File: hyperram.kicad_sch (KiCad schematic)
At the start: 7 parts

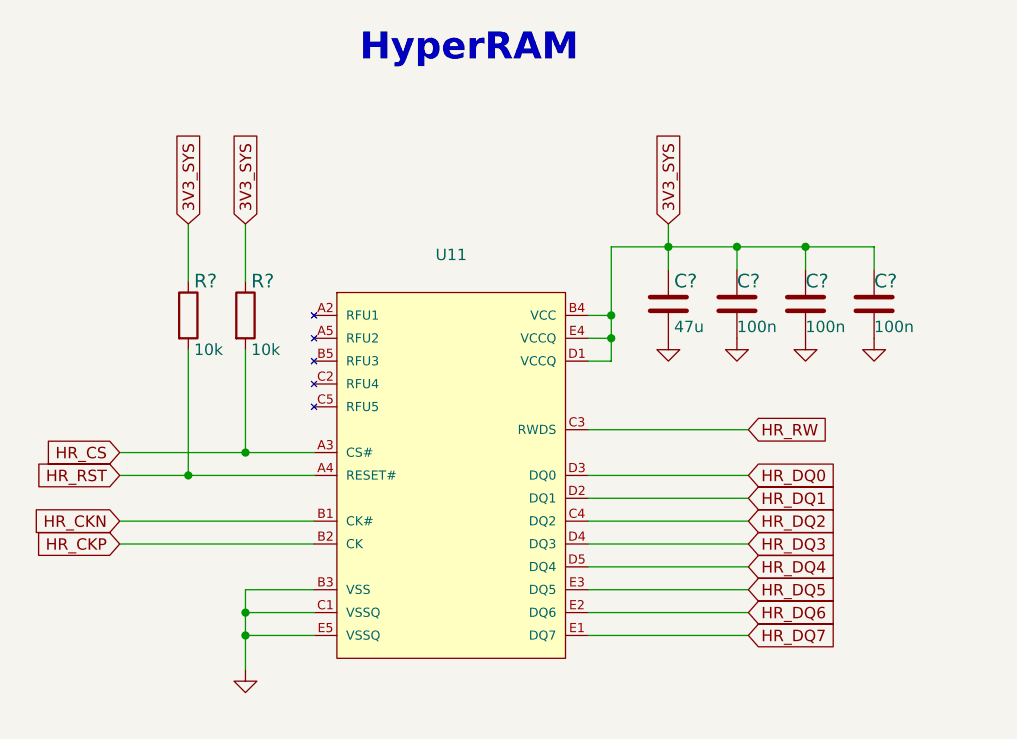
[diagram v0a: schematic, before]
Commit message: Added EN pullup for TPS54561 to avoid disabling by touch
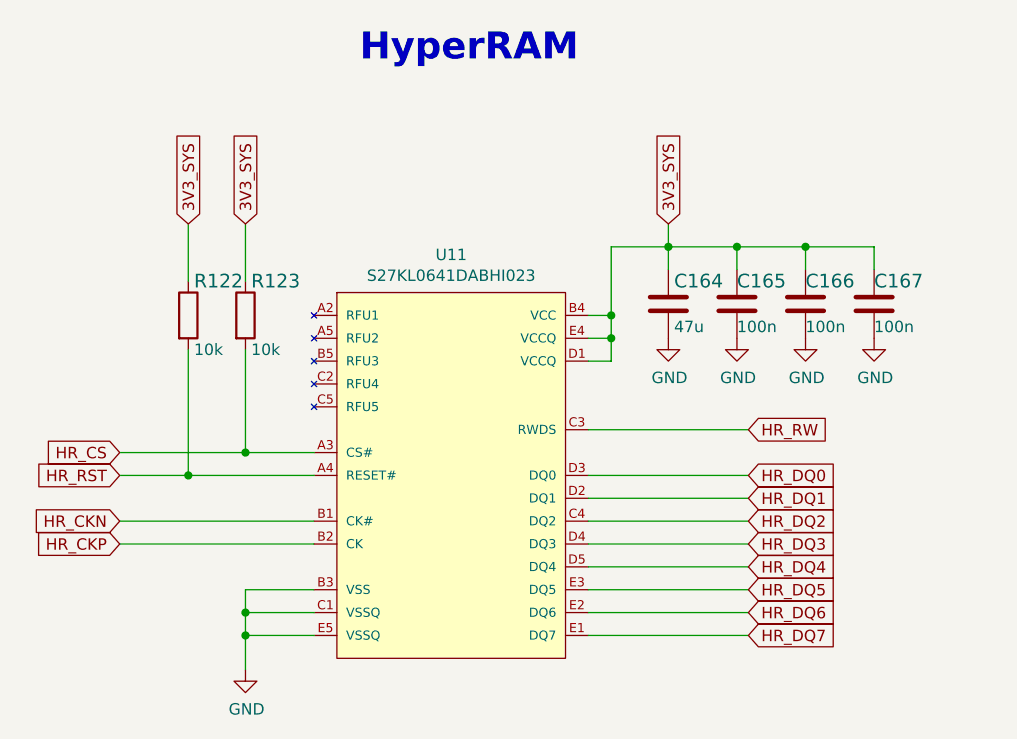
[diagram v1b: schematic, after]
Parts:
- C164: renamed from C?; value (none) -> C_47u_0603; footprint (none) -> ddr5-testboard-footprints:0603-cap
- C165, C166, C167: renamed from C?; value (none) -> C_100n_0402_6V3; footprint (none) -> ddr5-testboard-footprints:0402-cap
- R122, R123: renamed from R?; value (none) -> R_10k_0402; footprint (none) -> ddr5-testboard-footprints:0402-res
- U11: value (none) -> S27KL0641DABHI023; footprint (none) -> ddr5-testboard-footprints:FBGA-24
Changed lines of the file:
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@@
     (in_bom yes) (on_board yes)
     (property "Reference" "U11" (id 0) (at 196.215 125.984 0))
-    (property "Value" "" (id 1) (at 196.215 128.2954 0))
-    (property "Footprint" "" (id 2) (at 184.785 178.435 0)
+    (property "Value" "S27KL0641DABHI023" (id 1) (at 196.215 128.2954 0))
+    (property "Footprint" "ddr5-testboard-footprints:FBGA-24" (id 2) (at 184.785 178.435 0)
       (effects (font (size 1.27 1.27)) (justify left bottom) hide)
     )
@@
   (symbol (lib_id "ddr5-testboard:C_47u_0603") (at 220.345 131.445 0) (unit 1)
     (in_bom yes) (on_board yes)
-    (property "Reference" "C?" (id 0) (at 220.98 128.905 0)
-      (effects (font (size 1.524 1.524)) (justify left))
-    )
-    (property "Value" "" (id 1) (at 220.345 135.255 0)
-      (effects (font (size 1.524 1.524)) hide)
-    )
-    (property "Footprint" "" (id 2) (at 225.425 126.365 0)
+    (property "Reference" "C164" (id 0) (at 220.98 128.905 0)
+      (effects (font (size 1.524 1.524)) (justify left))
+    )
+    (property "Value" "C_47u_0603" (id 1) (at 220.345 135.255 0)
+      (effects (font (size 1.524 1.524)) hide)
+    )
+    (property "Footprint" "ddr5-testboard-footprints:0603-cap" (id 2) (at 225.425 126.365 0)
       (effects (font (size 1.524 1.524)) (justify left) hide)
     )
@@
   (symbol (lib_id "ddr5-testboard:C_100n_0402_6V3") (at 235.585 131.445 0) (unit 1)
     (in_bom yes) (on_board yes)
-    (property "Reference" "C?" (id 0) (at 235.585 128.905 0)
-      (effects (font (size 1.524 1.524)) (justify left))
-    )
-    (property "Value" "" (id 1) (at 235.585 135.255 0)
-      (effects (font (size 1.524 1.524)) hide)
-    )
-    (property "Footprint" "" (id 2) (at 240.665 126.365 0)
+    (property "Reference" "C166" (id 0) (at 235.585 128.905 0)
+      (effects (font (size 1.524 1.524)) (justify left))
+    )
+    (property "Value" "C_100n_0402_6V3" (id 1) (at 235.585 135.255 0)
+      (effects (font (size 1.524 1.524)) hide)
+    )
+    (property "Footprint" "ddr5-testboard-footprints:0402-cap" (id 2) (at 240.665 126.365 0)
       (effects (font (size 1.524 1.524)) (justify left) hide)
     )
@@
   (symbol (lib_id "ddr5-testboard:GND") (at 220.345 135.255 0) (unit 1)
     (in_bom yes) (on_board yes)
-    (property "Reference" "#PWR?" (id 0) (at 220.345 141.605 0)
-      (effects (font (size 1.27 1.27)) hide)
-    )
-    (property "Value" "" (id 1) (at 220.472 139.6492 0))
+    (property "Reference" "#PWR0189" (id 0) (at 220.345 141.605 0)
+      (effects (font (size 1.27 1.27)) hide)
+    )
+    (property "Value" "GND" (id 1) (at 220.472 139.6492 0))
     (property "Footprint" "" (id 2) (at 220.345 135.255 0)
       (effects (font (size 1.27 1.27)) hide)
@@
   (symbol (lib_id "ddr5-testboard:R_10k_0402") (at 167.005 132.715 270) (unit 1)
     (in_bom yes) (on_board yes)
-    (property "Reference" "R?" (id 0) (at 167.64 128.905 90)
-      (effects (font (size 1.524 1.524)) (justify left))
-    )
-    (property "Value" "" (id 1) (at 163.195 132.715 0)
-      (effects (font (size 1.524 1.524)) hide)
-    )
-    (property "Footprint" "" (id 2) (at 172.085 137.795 0)
+    (property "Reference" "R122" (id 0) (at 167.64 128.905 90)
+      (effects (font (size 1.524 1.524)) (justify left))
+    )
+    (property "Value" "R_10k_0402" (id 1) (at 163.195 132.715 0)
+      (effects (font (size 1.524 1.524)) hide)
+    )
+    (property "Footprint" "ddr5-testboard-footprints:0402-res" (id 2) (at 172.085 137.795 0)
       (effects (font (size 1.524 1.524)) (justify left) hide)
     )
@@
   (symbol (lib_id "ddr5-testboard:GND") (at 227.965 135.255 0) (unit 1)
     (in_bom yes) (on_board yes)
-    (property "Reference" "#PWR?" (id 0) (at 227.965 141.605 0)
-      (effects (font (size 1.27 1.27)) hide)
-    )
-    (property "Value" "" (id 1) (at 228.092 139.6492 0))
+    (property "Reference" "#PWR0190" (id 0) (at 227.965 141.605 0)
+      (effects (font (size 1.27 1.27)) hide)
+    )
+    (property "Value" "GND" (id 1) (at 228.092 139.6492 0))
     (property "Footprint" "" (id 2) (at 227.965 135.255 0)
       (effects (font (size 1.27 1.27)) hide)
@@
   (symbol (lib_id "ddr5-testboard:GND") (at 235.585 135.255 0) (unit 1)
     (in_bom yes) (on_board yes)
-    (property "Reference" "#PWR?" (id 0) (at 235.585 141.605 0)
-      (effects (font (size 1.27 1.27)) hide)
-    )
-    (property "Value" "" (id 1) (at 235.712 139.6492 0))
+    (property "Reference" "#PWR0191" (id 0) (at 235.585 141.605 0)
+      (effects (font (size 1.27 1.27)) hide)
+    )
+    (property "Value" "GND" (id 1) (at 235.712 139.6492 0))
     (property "Footprint" "" (id 2) (at 235.585 135.255 0)
       (effects (font (size 1.27 1.27)) hide)
@@
   (symbol (lib_id "ddr5-testboard:C_100n_0402_6V3") (at 227.965 131.445 0) (unit 1)
     (in_bom yes) (on_board yes)
-    (property "Reference" "C?" (id 0) (at 227.965 128.905 0)
-      (effects (font (size 1.524 1.524)) (justify left))
-    )
-    (property "Value" "" (id 1) (at 227.965 135.255 0)
-      (effects (font (size 1.524 1.524)) hide)
-    )
-    (property "Footprint" "" (id 2) (at 233.045 126.365 0)
+    (property "Reference" "C165" (id 0) (at 227.965 128.905 0)
+      (effects (font (size 1.524 1.524)) (justify left))
+    )
+    (property "Value" "C_100n_0402_6V3" (id 1) (at 227.965 135.255 0)
+      (effects (font (size 1.524 1.524)) hide)
+    )
+    (property "Footprint" "ddr5-testboard-footprints:0402-cap" (id 2) (at 233.045 126.365 0)
       (effects (font (size 1.524 1.524)) (justify left) hide)
     )
@@
   (symbol (lib_id "ddr5-testboard:R_10k_0402") (at 173.355 132.715 270) (unit 1)
     (in_bom yes) (on_board yes)
-    (property "Reference" "R?" (id 0) (at 173.99 128.905 90)
-      (effects (font (size 1.524 1.524)) (justify left))
-    )
-    (property "Value" "" (id 1) (at 169.545 132.715 0)
-      (effects (font (size 1.524 1.524)) hide)
-    )
-    (property "Footprint" "" (id 2) (at 178.435 137.795 0)
+    (property "Reference" "R123" (id 0) (at 173.99 128.905 90)
+      (effects (font (size 1.524 1.524)) (justify left))
+    )
+    (property "Value" "R_10k_0402" (id 1) (at 169.545 132.715 0)
+      (effects (font (size 1.524 1.524)) hide)
+    )
+    (property "Footprint" "ddr5-testboard-footprints:0402-res" (id 2) (at 178.435 137.795 0)
       (effects (font (size 1.524 1.524)) (justify left) hide)
     )
@@
   (symbol (lib_id "ddr5-testboard:GND") (at 173.355 172.085 0) (unit 1)
     (in_bom yes) (on_board yes)
-    (property "Reference" "#PWR?" (id 0) (at 173.355 178.435 0)
-      (effects (font (size 1.27 1.27)) hide)
-    )
-    (property "Value" "" (id 1) (at 173.482 176.4792 0))
+    (property "Reference" "#PWR0188" (id 0) (at 173.355 178.435 0)
+      (effects (font (size 1.27 1.27)) hide)
+    )
+    (property "Value" "GND" (id 1) (at 173.482 176.4792 0))
     (property "Footprint" "" (id 2) (at 173.355 172.085 0)
       (effects (font (size 1.27 1.27)) hide)
@@
   (symbol (lib_id "ddr5-testboard:C_100n_0402_6V3") (at 243.205 131.445 0) (unit 1)
     (in_bom yes) (on_board yes)
-    (property "Reference" "C?" (id 0) (at 243.205 128.905 0)
-      (effects (font (size 1.524 1.524)) (justify left))
-    )
-    (property "Value" "" (id 1) (at 243.205 135.255 0)
-      (effects (font (size 1.524 1.524)) hide)
-    )
-    (property "Footprint" "" (id 2) (at 248.285 126.365 0)
+    (property "Reference" "C167" (id 0) (at 243.205 128.905 0)
+      (effects (font (size 1.524 1.524)) (justify left))
+    )
+    (property "Value" "C_100n_0402_6V3" (id 1) (at 243.205 135.255 0)
+      (effects (font (size 1.524 1.524)) hide)
+    )
+    (property "Footprint" "ddr5-testboard-footprints:0402-cap" (id 2) (at 248.285 126.365 0)
       (effects (font (size 1.524 1.524)) (justify left) hide)
     )
@@
   (symbol (lib_id "ddr5-testboard:GND") (at 243.205 135.255 0) (unit 1)
     (in_bom yes) (on_board yes)
-    (property "Reference" "#PWR?" (id 0) (at 243.205 141.605 0)
-      (effects (font (size 1.27 1.27)) hide)
-    )
-    (property "Value" "" (id 1) (at 243.332 139.6492 0))
+    (property "Reference" "#PWR0192" (id 0) (at 243.205 141.605 0)
+      (effects (font (size 1.27 1.27)) hide)
+    )
+    (property "Value" "GND" (id 1) (at 243.332 139.6492 0))
     (property "Footprint" "" (id 2) (at 243.205 135.255 0)
       (effects (font (size 1.27 1.27)) hide)

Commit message: Update naming convention
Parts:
- C164: footprint ddr5-testboard-footprints:0603-cap -> data-center-rdimm-ddr5-tester-footprints:0603-cap; symbol ddr5-testboard:C_47u_0603 -> data-center-rdimm-ddr5-tester:C_47u_0603
- C165, C166, C167: footprint ddr5-testboard-footprints:0402-cap -> data-center-rdimm-ddr5-tester-footprints:0402-cap; symbol ddr5-testboard:C_100n_0402_6V3 -> data-center-rdimm-ddr5-tester:C_100n_0402_6V3
- R122, R123: footprint ddr5-testboard-footprints:0402-res -> data-center-rdimm-ddr5-tester-footprints:0402-res; symbol ddr5-testboard:R_10k_0402 -> data-center-rdimm-ddr5-tester:R_10k_0402
- U11: footprint ddr5-testboard-footprints:FBGA-24 -> data-center-rdimm-ddr5-tester-footprints:FBGA-24; symbol ddr5-testboard:S27KL0641DABHI023 -> data-center-rdimm-ddr5-tester:S27KL0641DABHI023
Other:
- title: DDR5 Tester -> Data Center RDIMM DDR5 Tester
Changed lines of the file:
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@@
   (paper "A3")
   (title_block
-    (title "DDR5 Tester")
+    (title "Data Center RDIMM DDR5 Tester")
     (date "2022-03-08")
     (rev "1.0.0")
@@
     )
   )
-  (symbol (lib_id "ddr5-testboard:S27KL0641DABHI023") (at 196.215 150.495 0) (unit 1)
+  (symbol (lib_id "data-center-rdimm-ddr5-tester:S27KL0641DABHI023") (at 196.215 150.495 0) (unit 1)
     (in_bom yes) (on_board yes)
     (property "Reference" "U11" (id 0) (at 196.215 125.984 0))
     (property "Value" "S27KL0641DABHI023" (id 1) (at 196.215 128.2954 0))
-    (property "Footprint" "ddr5-testboard-footprints:FBGA-24" (id 2) (at 184.785 178.435 0)
+    (property "Footprint" "data-center-rdimm-ddr5-tester-footprints:FBGA-24" (id 2) (at 184.785 178.435 0)
       (effects (font (size 1.27 1.27)) (justify left bottom) hide)
     )
@@
     (pin "B2")
   )
-  (symbol (lib_id "ddr5-testboard:C_47u_0603") (at 220.345 131.445 0) (unit 1)
+  (symbol (lib_id "data-center-rdimm-ddr5-tester:C_47u_0603") (at 220.345 131.445 0) (unit 1)
     (in_bom yes) (on_board yes)
     (property "Reference" "C164" (id 0) (at 220.98 128.905 0)
@@
       (effects (font (size 1.524 1.524)) hide)
     )
-    (property "Footprint" "ddr5-testboard-footprints:0603-cap" (id 2) (at 225.425 126.365 0)
+    (property "Footprint" "data-center-rdimm-ddr5-tester-footprints:0603-cap" (id 2) (at 225.425 126.365 0)
       (effects (font (size 1.524 1.524)) (justify left) hide)
     )
@@
     (pin "2")
   )
-  (symbol (lib_id "ddr5-testboard:C_100n_0402_6V3") (at 235.585 131.445 0) (unit 1)
+  (symbol (lib_id "data-center-rdimm-ddr5-tester:C_100n_0402_6V3") (at 235.585 131.445 0) (unit 1)
     (in_bom yes) (on_board yes)
     (property "Reference" "C166" (id 0) (at 235.585 128.905 0)
@@
       (effects (font (size 1.524 1.524)) hide)
     )
-    (property "Footprint" "ddr5-testboard-footprints:0402-cap" (id 2) (at 240.665 126.365 0)
+    (property "Footprint" "data-center-rdimm-ddr5-tester-footprints:0402-cap" (id 2) (at 240.665 126.365 0)
       (effects (font (size 1.524 1.524)) (justify left) hide)
     )
@@
     (pin "2")
   )
-  (symbol (lib_id "ddr5-testboard:GND") (at 220.345 135.255 0) (unit 1)
+  (symbol (lib_id "data-center-rdimm-ddr5-tester:GND") (at 220.345 135.255 0) (unit 1)
     (in_bom yes) (on_board yes)
     (property "Reference" "#PWR0189" (id 0) (at 220.345 141.605 0)
@@
     (pin "1")
   )
-  (symbol (lib_id "ddr5-testboard:R_10k_0402") (at 167.005 132.715 270) (unit 1)
+  (symbol (lib_id "data-center-rdimm-ddr5-tester:R_10k_0402") (at 167.005 132.715 270) (unit 1)
     (in_bom yes) (on_board yes)
     (property "Reference" "R122" (id 0) (at 167.64 128.905 90)
@@
       (effects (font (size 1.524 1.524)) hide)
     )
-    (property "Footprint" "ddr5-testboard-footprints:0402-res" (id 2) (at 172.085 137.795 0)
+    (property "Footprint" "data-center-rdimm-ddr5-tester-footprints:0402-res" (id 2) (at 172.085 137.795 0)
       (effects (font (size 1.524 1.524)) (justify left) hide)
     )
@@
     (pin "2")
   )
-  (symbol (lib_id "ddr5-testboard:GND") (at 227.965 135.255 0) (unit 1)
+  (symbol (lib_id "data-center-rdimm-ddr5-tester:GND") (at 227.965 135.255 0) (unit 1)
     (in_bom yes) (on_board yes)
     (property "Reference" "#PWR0190" (id 0) (at 227.965 141.605 0)
@@
     (pin "1")
   )
-  (symbol (lib_id "ddr5-testboard:GND") (at 235.585 135.255 0) (unit 1)
+  (symbol (lib_id "data-center-rdimm-ddr5-tester:GND") (at 235.585 135.255 0) (unit 1)
     (in_bom yes) (on_board yes)
     (property "Reference" "#PWR0191" (id 0) (at 235.585 141.605 0)
@@
     (pin "1")
   )
-  (symbol (lib_id "ddr5-testboard:C_100n_0402_6V3") (at 227.965 131.445 0) (unit 1)
+  (symbol (lib_id "data-center-rdimm-ddr5-tester:C_100n_0402_6V3") (at 227.965 131.445 0) (unit 1)
     (in_bom yes) (on_board yes)
     (property "Reference" "C165" (id 0) (at 227.965 128.905 0)
@@
       (effects (font (size 1.524 1.524)) hide)
     )
-    (property "Footprint" "ddr5-testboard-footprints:0402-cap" (id 2) (at 233.045 126.365 0)
+    (property "Footprint" "data-center-rdimm-ddr5-tester-footprints:0402-cap" (id 2) (at 233.045 126.365 0)
       (effects (font (size 1.524 1.524)) (justify left) hide)
     )
@@
     (pin "2")
   )
-  (symbol (lib_id "ddr5-testboard:R_10k_0402") (at 173.355 132.715 270) (unit 1)
+  (symbol (lib_id "data-center-rdimm-ddr5-tester:R_10k_0402") (at 173.355 132.715 270) (unit 1)
     (in_bom yes) (on_board yes)
     (property "Reference" "R123" (id 0) (at 173.99 128.905 90)
@@
       (effects (font (size 1.524 1.524)) hide)
     )
-    (property "Footprint" "ddr5-testboard-footprints:0402-res" (id 2) (at 178.435 137.795 0)
+    (property "Footprint" "data-center-rdimm-ddr5-tester-footprints:0402-res" (id 2) (at 178.435 137.795 0)
       (effects (font (size 1.524 1.524)) (justify left) hide)
     )
@@
     (pin "2")
   )
-  (symbol (lib_id "ddr5-testboard:GND") (at 173.355 172.085 0) (unit 1)
+  (symbol (lib_id "data-center-rdimm-ddr5-tester:GND") (at 173.355 172.085 0) (unit 1)
     (in_bom yes) (on_board yes)
     (property "Reference" "#PWR0188" (id 0) (at 173.355 178.435 0)
@@
     (pin "1")
   )
-  (symbol (lib_id "ddr5-testboard:C_100n_0402_6V3") (at 243.205 131.445 0) (unit 1)
+  (symbol (lib_id "data-center-rdimm-ddr5-tester:C_100n_0402_6V3") (at 243.205 131.445 0) (unit 1)
     (in_bom yes) (on_board yes)
     (property "Reference" "C167" (id 0) (at 243.205 128.905 0)
@@
       (effects (font (size 1.524 1.524)) hide)
     )
-    (property "Footprint" "ddr5-testboard-footprints:0402-cap" (id 2) (at 248.285 126.365 0)
+    (property "Footprint" "data-center-rdimm-ddr5-tester-footprints:0402-cap" (id 2) (at 248.285 126.365 0)
       (effects (font (size 1.524 1.524)) (justify left) hide)
     )
@@
     (pin "2")
   )
-  (symbol (lib_id "ddr5-testboard:GND") (at 243.205 135.255 0) (unit 1)
+  (symbol (lib_id "data-center-rdimm-ddr5-tester:GND") (at 243.205 135.255 0) (unit 1)
     (in_bom yes) (on_board yes)
     (property "Reference" "#PWR0192" (id 0) (at 243.205 141.605 0)
